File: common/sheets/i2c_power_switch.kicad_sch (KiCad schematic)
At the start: 7 parts, among them U4 MCP23008T-E/SS, U5 INA226AIDGSR

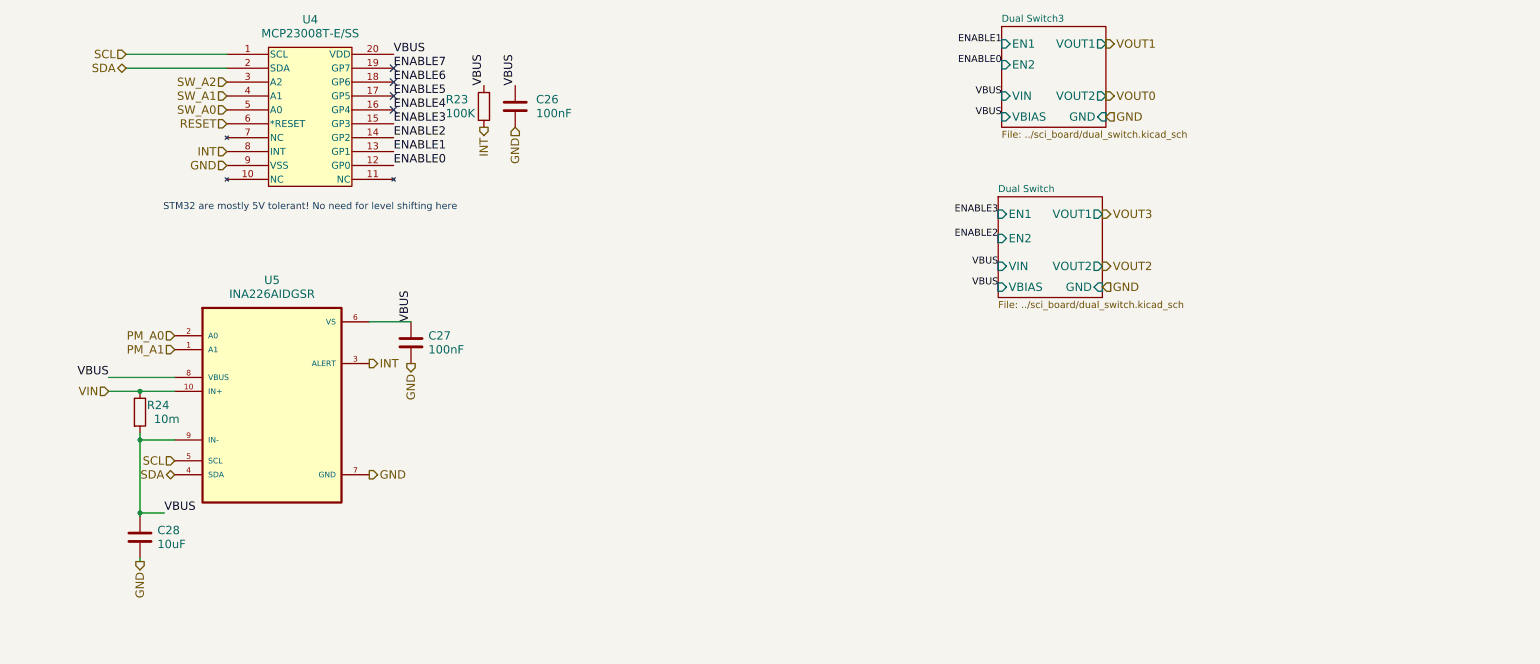
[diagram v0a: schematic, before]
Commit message: move commonly used hierarchical sheets to common/sheets for easy reuse
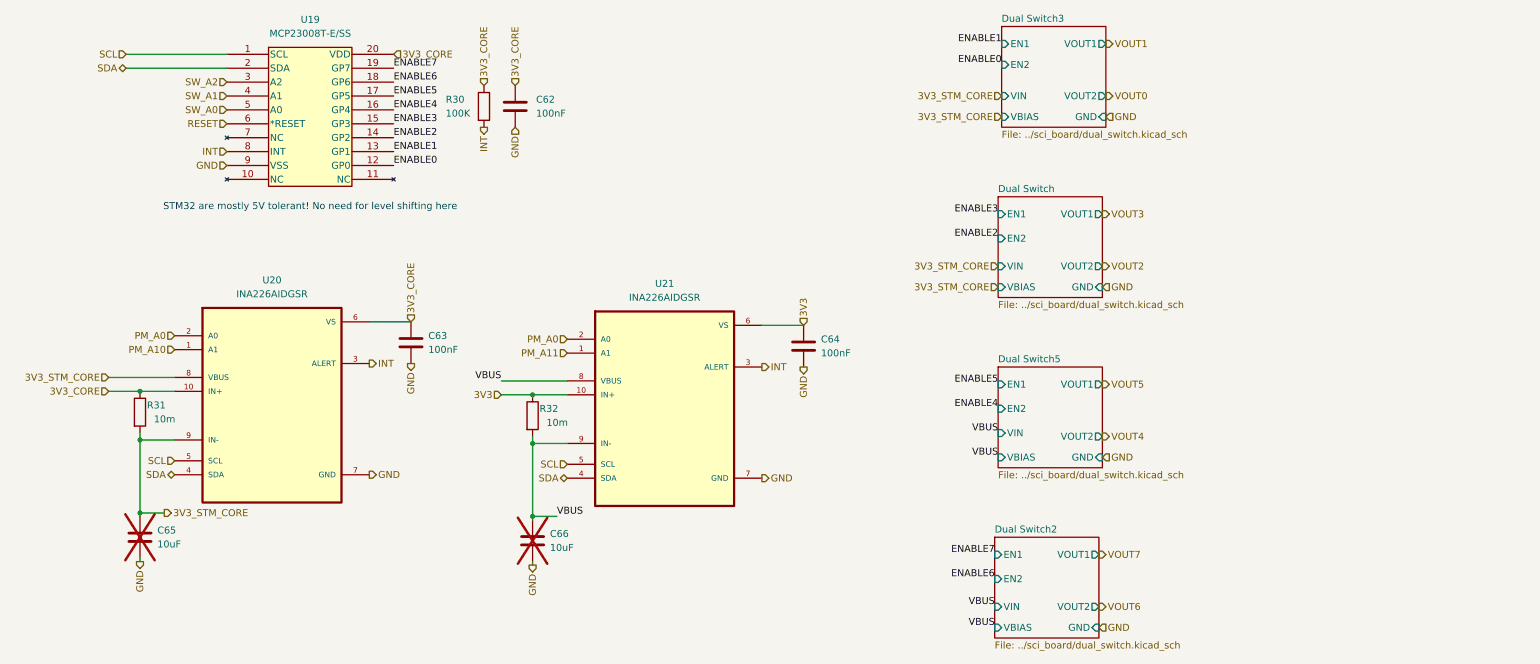
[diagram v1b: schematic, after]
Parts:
- added C64: 100nF, Capacitor_SMD:C_0402_1005Metric_Pad0.74x0.62mm_HandSolder, symbol Device:C
- added C66: 10uF, Capacitor_SMD:C_0603_1608Metric_Pad1.08x0.95mm_HandSolder, symbol Device:C
- added R32: 10m, Resistor_SMD:R_0805_2012Metric_Pad1.20x1.40mm_HandSolder, symbol Device:R
- added U21: INA226AIDGSR, Package_SO:VSSOP-10_3x3mm_P0.5mm, symbol Common:INA226AIDGSR
- C65: renamed from C28; now not fitted
- renumbered C26 to C62, C27 to C63, R23 to R30, R24 to R31, U4 to U19, U5 to U20
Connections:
- net GND: now also C64.2, C66.2, U21.7 (GND)
- net INT: now also U21.3 (ALERT)
- net PM_A0: now also U21.2 (A0)
- net SCL: now also U21.5 (SCL)
- net SDA: now also U21.4 (SDA)
- net VBUS: now also C66.1, R32.2, U21.8 (VBUS), U21.9 (IN-); no longer C62.1, C63.1, C65.1, R30.1, R31.2, U19.20 (VDD), U20.6 (VS), U20.8 (VBUS), U20.9 (IN-)
- net PM_A1 renamed PM_A10
- net VIN renamed 3V3_CORE
- net 3V3_CORE: now also C62.1, C63.1, R30.1, U19.20 (VDD), U20.6 (VS)
- new net 3V3: C64.1, R32.1, U21.10 (IN+), U21.6 (VS)
- new net 3V3_STM_CORE: C65.1, R31.2, U20.8 (VBUS), U20.9 (IN-)
- new net PM_A11: U21.1 (A1)
- no-connect marks 4 -> 0
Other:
- added sheet Dual Switch2 (../sci_board/dual_switch.kicad_sch)
- added sheet Dual Switch5 (../sci_board/dual_switch.kicad_sch)

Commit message: absolute paths for includes of includes or the second level common/sheet will cause problems!
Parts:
- renumbered C64 to C100, C65 to C101, C66 to C102, C62 to C98, C63 to C99, R30 to R31, R31 to R32, R32 to R33, U19 to U25, U20 to U26, U21 to U27
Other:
- sheet Dual Switch: file ../sci_board/dual_switch.kicad_sch -> /home/mgi/Data/kicad/Hardware_CSAT/common/sheets/dual_switch.kicad_sch
- sheet Dual Switch2: file ../sci_board/dual_switch.kicad_sch -> /home/mgi/Data/kicad/Hardware_CSAT/common/sheets/dual_switch.kicad_sch
- sheet Dual Switch3: file ../sci_board/dual_switch.kicad_sch -> /home/mgi/Data/kicad/Hardware_CSAT/common/sheets/dual_switch.kicad_sch
- sheet Dual Switch5: file ../sci_board/dual_switch.kicad_sch -> /home/mgi/Data/kicad/Hardware_CSAT/common/sheets/dual_switch.kicad_sch
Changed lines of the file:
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@@
 		(dnp yes)
 		(fields_autoplaced yes)
-		(property "Reference" "C65"
+		(property "Reference" "C101"
 			(at 52.07 118.7449 0)
 			(effects
@@
 			(project "EPS"
 				(path "/05170af6-30ef-4c3a-b972-f098085da1bc/53211e67-c677-4be8-893d-9825fa308902"
-					(reference "C65")
+					(reference "C101")
 					(unit 1)
 				)
@@
 		(dnp no)
 		(fields_autoplaced yes)
-		(property "Reference" "C62"
+		(property "Reference" "C98"
 			(at 121.285 40.0049 0)
 			(effects
@@
 			(project "EPS"
 				(path "/05170af6-30ef-4c3a-b972-f098085da1bc/53211e67-c677-4be8-893d-9825fa308902"
-					(reference "C62")
+					(reference "C98")
 					(unit 1)
 				)
@@
 		(on_board yes)
 		(dnp no)
-		(property "Reference" "R30"
+		(property "Reference" "R31"
 			(at 104.775 40.005 0)
 			(effects
@@
 			(project "EPS"
 				(path "/05170af6-30ef-4c3a-b972-f098085da1bc/53211e67-c677-4be8-893d-9825fa308902"
-					(reference "R30")
+					(reference "R31")
 					(unit 1)
 				)
@@
 		(on_board yes)
 		(dnp no)
-		(property "Reference" "R32"
+		(property "Reference" "R33"
 			(at 121.92 96.52 0)
 			(effects
@@
 			(project "EPS"
 				(path "/05170af6-30ef-4c3a-b972-f098085da1bc/53211e67-c677-4be8-893d-9825fa308902"
-					(reference "R32")
+					(reference "R33")
 					(unit 1)
 				)
@@
 		(dnp no)
 		(fields_autoplaced yes)
-		(property "Reference" "U20"
+		(property "Reference" "U26"
 			(at 73.025 73.025 0)
 			(effects
@@
 			(project "EPS"
 				(path "/05170af6-30ef-4c3a-b972-f098085da1bc/53211e67-c677-4be8-893d-9825fa308902"
-					(reference "U20")
+					(reference "U26")
 					(unit 1)
 				)
@@
 		(dnp no)
 		(fields_autoplaced yes)
-		(property "Reference" "C64"
+		(property "Reference" "C100"
 			(at 173.355 83.8199 0)
 			(effects
@@
 			(project "EPS"
 				(path "/05170af6-30ef-4c3a-b972-f098085da1bc/53211e67-c677-4be8-893d-9825fa308902"
-					(reference "C64")
+					(reference "C100")
 					(unit 1)
 				)
@@
 		(on_board yes)
 		(dnp no)
-		(property "Reference" "R31"
+		(property "Reference" "R32"
 			(at 50.165 95.885 0)
 			(effects
@@
 			(project "EPS"
 				(path "/05170af6-30ef-4c3a-b972-f098085da1bc/53211e67-c677-4be8-893d-9825fa308902"
-					(reference "R31")
+					(reference "R32")
 					(unit 1)
 				)
@@
 		(dnp no)
 		(fields_autoplaced yes)
-		(property "Reference" "U19"
+		(property "Reference" "U25"
 			(at 80.01 25.4 0)
 			(effects
@@
 			(project "EPS"
 				(path "/05170af6-30ef-4c3a-b972-f098085da1bc/53211e67-c677-4be8-893d-9825fa308902"
-					(reference "U19")
+					(reference "U25")
 					(unit 1)
 				)
@@
 		(dnp yes)
 		(fields_autoplaced yes)
-		(property "Reference" "C66"
+		(property "Reference" "C102"
 			(at 123.825 119.3799 0)
 			(effects
@@
 			(project "EPS"
 				(path "/05170af6-30ef-4c3a-b972-f098085da1bc/53211e67-c677-4be8-893d-9825fa308902"
-					(reference "C66")
+					(reference "C102")
 					(unit 1)
 				)
@@
 		(dnp no)
 		(fields_autoplaced yes)
-		(property "Reference" "U21"
+		(property "Reference" "U27"
 			(at 144.78 73.66 0)
 			(effects
@@
 			(project "EPS"
 				(path "/05170af6-30ef-4c3a-b972-f098085da1bc/53211e67-c677-4be8-893d-9825fa308902"
-					(reference "U21")
+					(reference "U27")
 					(unit 1)
 				)
@@
 		(dnp no)
 		(fields_autoplaced yes)
-		(property "Reference" "C63"
+		(property "Reference" "C99"
 			(at 101.6 83.1849 0)
 			(effects
@@
 			(project "EPS"
 				(path "/05170af6-30ef-4c3a-b972-f098085da1bc/53211e67-c677-4be8-893d-9825fa308902"
-					(reference "C63")
+					(reference "C99")
 					(unit 1)
 				)
@@
 			)
 		)
-		(property "Sheetfile" "../sci_board/dual_switch.kicad_sch"
+		(property "Sheetfile" "/home/mgi/Data/kicad/Hardware_CSAT/common/sheets/dual_switch.kicad_sch"
 			(at 206.375 45.6696 0)
 			(effects
@@
 				(path "/b4b2c88d-f6cd-4e60-862d-e21f68728580/bffa887c-2d4a-4897-aa07-de3665bc885a"
 					(page "11")
+				)
+			)
+			(project "EPS"
+				(path "/05170af6-30ef-4c3a-b972-f098085da1bc/53211e67-c677-4be8-893d-9825fa308902"
+					(page "#")
 				)
 			)
@@
 			)
 		)
-		(property "Sheetfile" "../sci_board/dual_switch.kicad_sch"
+		(property "Sheetfile" "/home/mgi/Data/kicad/Hardware_CSAT/common/sheets/dual_switch.kicad_sch"
 			(at 205.105 139.0146 0)
 			(effects
@@
 			)
 		)
-		(property "Sheetfile" "../sci_board/dual_switch.kicad_sch"
+		(property "Sheetfile" "/home/mgi/Data/kicad/Hardware_CSAT/common/sheets/dual_switch.kicad_sch"
 			(at 205.74 107.8996 0)
 			(effects
@@
 			)
 		)
-		(property "Sheetfile" "../sci_board/dual_switch.kicad_sch"
+		(property "Sheetfile" "/home/mgi/Data/kicad/Hardware_CSAT/common/sheets/dual_switch.kicad_sch"
 			(at 205.74 76.7846 0)
 			(effects
@@
 				)
 			)
+			(project "EPS"
+				(path "/05170af6-30ef-4c3a-b972-f098085da1bc/53211e67-c677-4be8-893d-9825fa308902"
+					(page "#")
+				)
+			)
